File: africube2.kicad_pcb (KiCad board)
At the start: 4 copper layers, 66 x 57 mm, 29 parts, among them J1 SMA Edge FM, J2 Conn_01x04, J3 RPi_GPIO, U1 TQP7M9105, U2 SXBP-150+, U3 BA178M05FP-E2

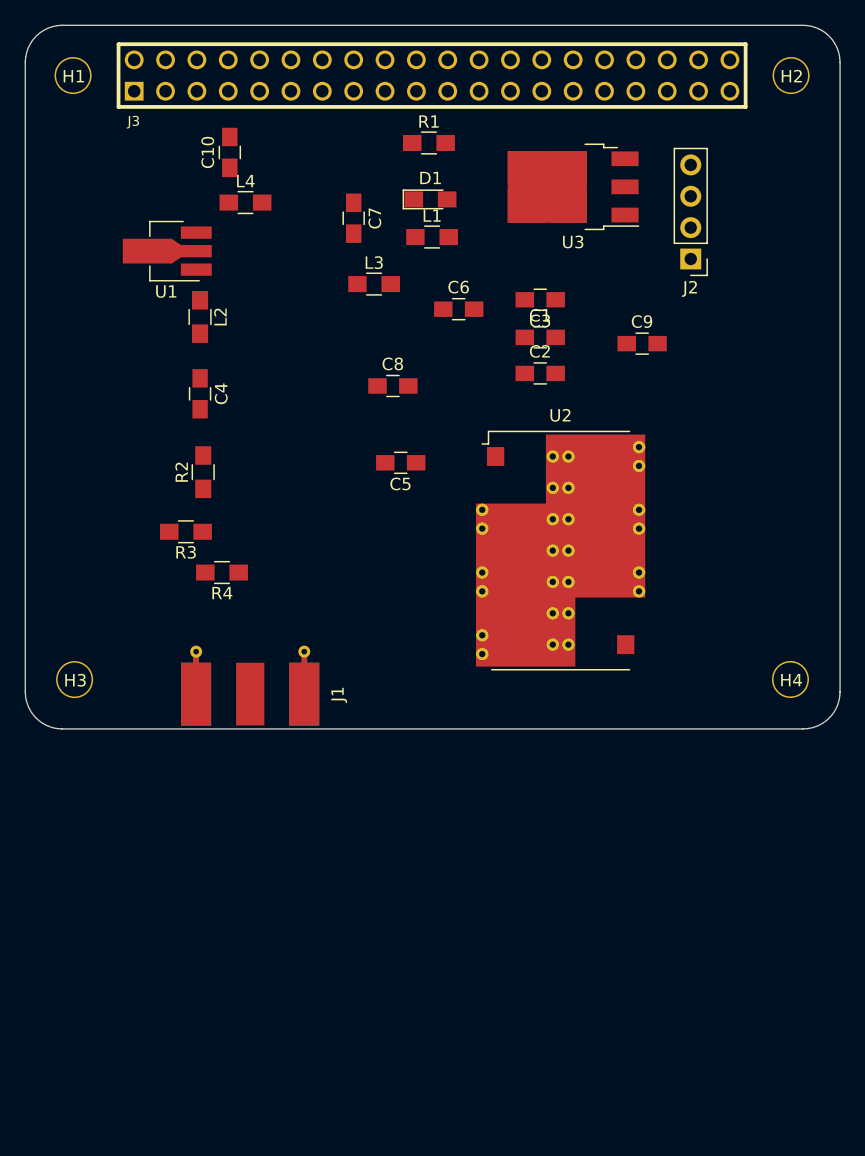
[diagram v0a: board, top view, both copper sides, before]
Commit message: adding directional copler
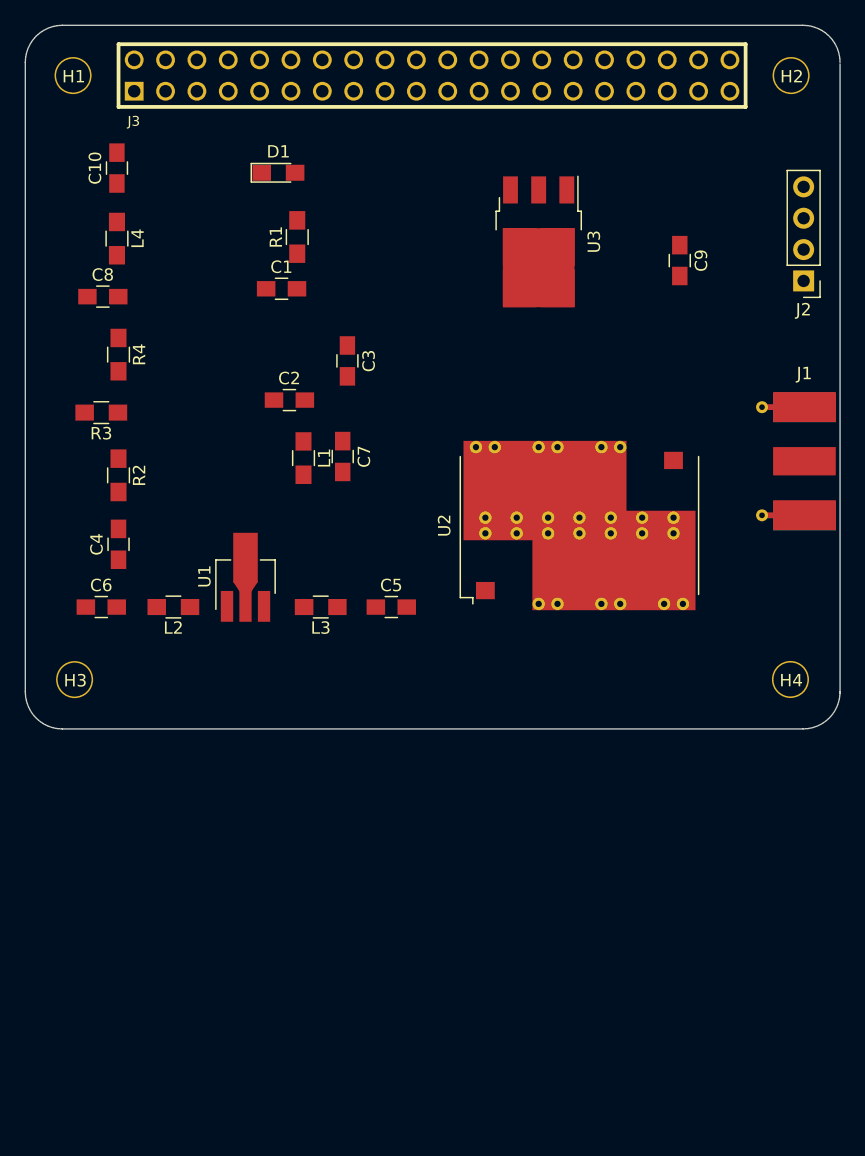
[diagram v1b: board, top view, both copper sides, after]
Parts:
- moved J1 46.5 mm to (139.4, 95.6), turned to 180 degrees
- moved C6 37.7 mm to (84.2, 107.4)
- moved U1 27.5 mm to (95.9, 105.4), turned to 90 degrees
- moved L3 26.5 mm to (102.0, 107.4), turned to 180 degrees
- moved C8 24.6 mm to (84.3, 82.3)
- moved L2 23.6 mm to (90.0, 107.4), turned to 180 degrees
- moved C1 21.3 mm to (98.8, 81.7)
- moved L1 20.7 mm to (100.6, 95.4), turned to 270 degrees
- moved C2 20.4 mm to (99.4, 90.7)
- moved R4 19.5 mm to (85.6, 87.0), turned to 270 degrees
- moved C7 19.3 mm to (103.8, 95.2)
- moved C3 16.4 mm to (104.1, 87.5), turned to 270 degrees
- moved C4 13.9 mm to (85.6, 102.4), turned to 90 degrees
- moved R1 13.1 mm to (100.1, 77.5), turned to 90 degrees
- moved D1 12.5 mm to (98.6, 72.3)
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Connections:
- C6 pad 2: (no net) -> Net-(C4-Pad1)
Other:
- outline, holes or cut-outs redrawn

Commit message: placing board
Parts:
- removed H1, H2: 3mm_Mounting_Hole, project_footprints:NPTH_3mm_ID
- added C11: 100pF, Capacitors_SMD:C_0805_HandSoldering, F.Cu at (85.5, 71.8)
- added C12: 1nF, Capacitors_SMD:C_0805_HandSoldering, F.Cu at (109.9, 89.5)
- added D2: SMS3922-079LF, Diodes_SMD:D_SOD-523, F.Cu at (94.1, 89.0)
- added IC1: ADC-20-4, rf_noise:ADC-20-4+, F.Cu at (132.7, 86.0)
- added J4: Conn_01x02, Pin_Headers:Pin_Header_Straight_1x02_Pitch2.54mm, F.Cu at (93.6, 73.8)
- added R5: 0, Resistors_SMD:R_0805_HandSoldering, F.Cu at (93.6, 82.9)
- added R6: 220K, Resistors_SMD:R_0805_HandSoldering, F.Cu at (99.7, 85.5)
- added R7: 220K, Resistors_SMD:R_0805_HandSoldering, F.Cu at (107.3, 80.4)
- added R8: 220K, Resistors_SMD:R_0805_HandSoldering, F.Cu at (107.3, 83.4)
- added R9: 220K, Resistors_SMD:R_0805_HandSoldering, F.Cu at (109.9, 86.5)
- added U4: MCP3421A0T-E/CH, TO_SOT_Packages_SMD:SOT-23-6_Handsoldering, F.Cu at (107.8, 74.8)
- C10: value 100pF -> 4.7uF 16V
- C8: value 10pF -> 100pF
- C9: value 4.7uF 16V -> 10pF
- J3: footprint HF_NOISE:PIN_ARRAY_20X2 -> Socket_Strips:Socket_Strip_Straight_2x20_Pitch2.54mm
- R3: value OC -> 50
- R4: value 0 -> OC
- moved C9 43.2 mm to (88.0, 82.9), turned to 90 degrees
- moved C10 36.6 mm to (122.0, 69.7)
- moved J3 23.1 mm to (88.0, 62.6), turned to 90 degrees
- moved J1 15.2 mm to (139.3, 80.4)
- moved J2 14.6 mm to (127.1, 76.8)
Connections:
- C10 pad 2: Net-(C10-Pad2) -> GND
- C8 pad 1: GND -> Net-(C8-Pad1)
- C9 pad 1: Net-(C9-Pad1) -> GND
- C9 pad 2: GND -> Net-(C9-Pad2)
- J1 pad 1: Net-(J1-Pad1) -> Net-(IC1-Pad6)
- J2 pad 2: Net-(J2-Pad2) -> Net-(C10-Pad1)
- J2 pad 3: Net-(C9-Pad1) -> +5V
- J2 pad 4: +5V -> Net-(J2-Pad4)
- J3 pad 1: Net-(J2-Pad2) -> Net-(J2-Pad4)
- J3 pad 17: Net-(J2-Pad2) -> Net-(J2-Pad4)
- J3 pad 2: +5V -> Net-(J3-Pad2)
- J3 pad 3: (no net) -> SDA
- J3 pad 4: +5V -> Net-(J3-Pad2)
- J3 pad 5: (no net) -> SCL
- J3 pad 7: Net-(C10-Pad2) -> Net-(C11-Pad2)
- L4 pad 1: Net-(C10-Pad1) -> Net-(C11-Pad1)
- L4 pad 2: Net-(C8-Pad2) -> Net-(C9-Pad2)
- R3 pad 1: Net-(R2-Pad1) -> Net-(IC1-Pad4)
- R4 pad 1: Net-(C8-Pad2) -> Net-(R2-Pad1)
- R4 pad 2: Net-(R2-Pad1) -> GND
- U2 pad 8: Net-(J1-Pad1) -> Net-(IC1-Pad1)
- U3 pad 1: Net-(C9-Pad1) -> Net-(C10-Pad1)

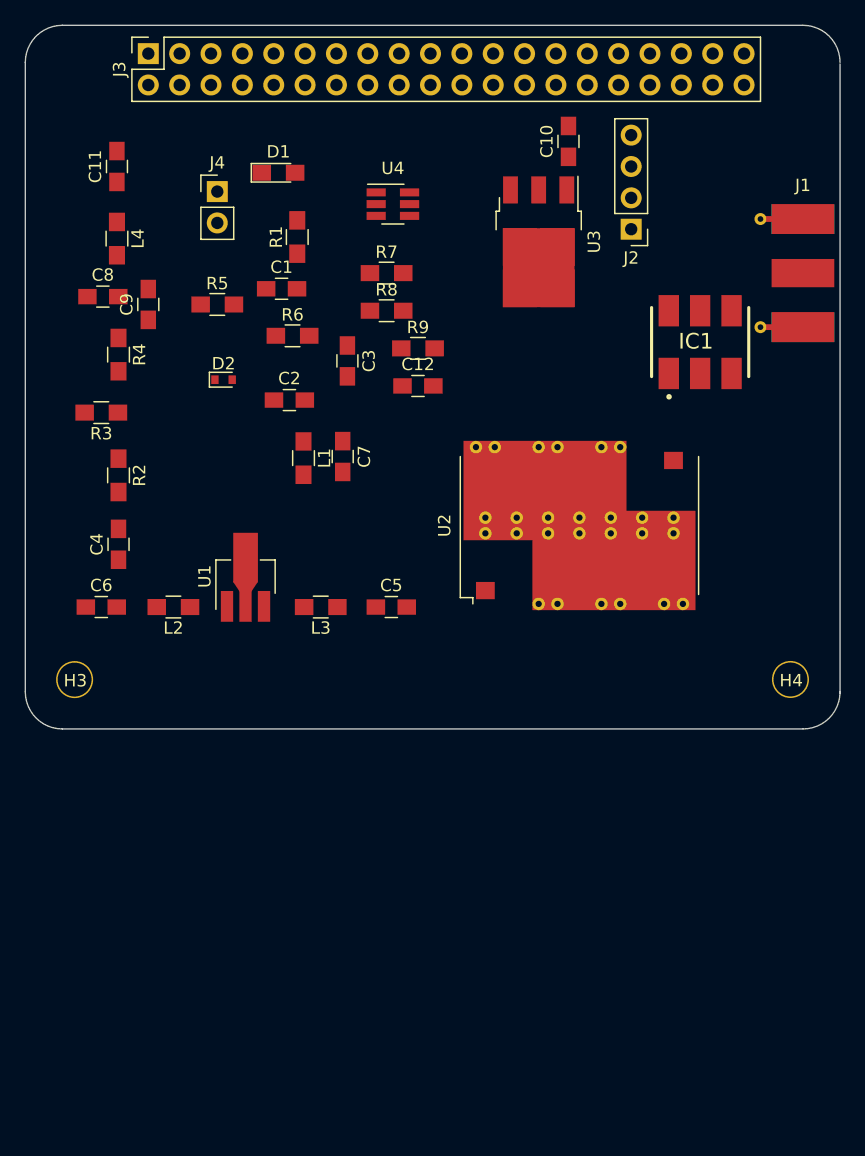
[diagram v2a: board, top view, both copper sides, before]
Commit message: Making pcb Bigger
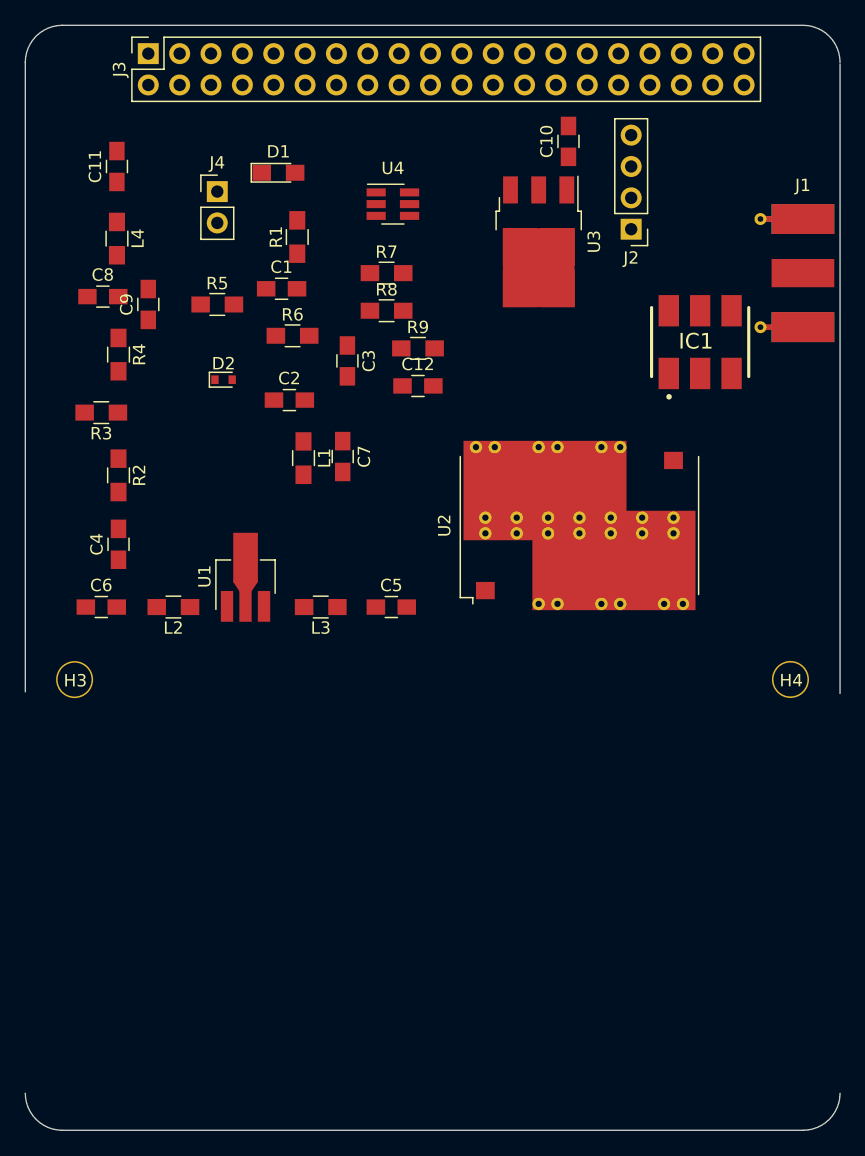
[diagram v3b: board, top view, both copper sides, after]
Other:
- board size 66 x 57 mm -> 66 x 89.5 mm
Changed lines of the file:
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@@
     (links 116)
     (no_connects 80)
-    (area 74.244762 60.071 171.553 149.987001)
+    (area 74.244762 49.751 171.553 149.987001)
     (thickness 1.6)
     (drawings 15)
@@
   (gr_circle (center 82.046356 64.317611) (end 83.421356 64.317611) (layer Dwgs.User) (width 0.1))
   (gr_circle (center 82.046356 113.317611) (end 83.421356 113.317611) (layer Dwgs.User) (width 0.1))
-  (gr_arc (start 81.046356 114.317611) (end 78.046356 114.317611) (angle -90) (layer Edge.Cuts) (width 0.1))
-  (gr_line (start 81.046356 117.317611) (end 141.046356 117.317611) (layer Edge.Cuts) (width 0.1))
-  (gr_arc (start 141.046356 114.317611) (end 141.046356 117.317611) (angle -89.9) (layer Edge.Cuts) (width 0.1))
+  (gr_arc (start 81.046356 146.829611) (end 78.046356 146.829611) (angle -90) (layer Edge.Cuts) (width 0.1))
+  (gr_line (start 81.046356 149.829611) (end 141.046356 149.829611) (layer Edge.Cuts) (width 0.1))
+  (gr_arc (start 141.046356 146.829611) (end 141.046356 149.829611) (angle -89.9) (layer Edge.Cuts) (width 0.1))
 )
